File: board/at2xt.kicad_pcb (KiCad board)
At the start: 2 copper layers, 45.7 x 39.4 mm, 15 parts, among them J1 Conn_01x04, J2 XT, J3 AT, J4 PS/2, U1 MCP1700-3302E_TO92, U2 MSP430G2211IPW14

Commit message: Apply some suggestions from dragonmux's hoard.
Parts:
- moved C4 8.47 mm to (158.8, 64.8)
- moved C1 1.96 mm to (163.2, 62.2)
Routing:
- net +3.3V: track 73.4 -> 58.6 mm, vias 3 -> 2
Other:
- board text added: "TDIO VTGT TCK GND"
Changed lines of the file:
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@@
   )
   (footprint "Capacitor_SMD:C_0603_1608Metric" (layer "F.Cu")
-    (at 164.90942 58.955)
+    (at 158.75 64.77)
     (descr "Capacitor SMD 0603 (1608 Metric), square (rectangular) end terminal, IPC_7351 nominal, (Body size source: IPC-SM-782 page 76, https://www.pcb-3d.com/wordpress/wp-content/uploads/ipc-sm-782a_amendment_1_and_2.pdf), generated with kicad-footprint-generator")
     (tags "capacitor")
@@
   )
   (footprint "Capacitor_SMD:C_0603_1608Metric" (layer "F.Cu")
-    (at 165.1 61.955)
+    (at 163.16 62.23)
     (descr "Capacitor SMD 0603 (1608 Metric), square (rectangular) end terminal, IPC_7351 nominal, (Body size source: IPC-SM-782 page 76, https://www.pcb-3d.com/wordpress/wp-content/uploads/ipc-sm-782a_amendment_1_and_2.pdf), generated with kicad-footprint-generator")
     (tags "capacitor")
@@
   (gr_line (start 121.92 91.44) (end 167.64 91.44) (layer "Edge.Cuts") (width 0.1))
   (gr_line (start 167.64 91.44) (end 167.64 52.07) (layer "Edge.Cuts") (width 0.1))
-  (segment (start 164.465 64.135) (end 163.195 65.405) (width 0.25) (layer "F.Cu") (net 1))
-  (segment (start 163.195 65.405) (end 159.6525 65.405) (width 0.25) (layer "F.Cu") (net 1))
-  (segment (start 164.13442 58.955) (end 164.465 59.28558) (width 0.25) (layer "F.Cu") (net 1))
+  (gr_text "TDIO\nVTGT\nTCK\nGND" (at 129.54 64.135) (layer "B.SilkS")
+    (effects (font (size 1.5 1.5) (thickness 0.3)) (justify mirror))
+  )
+  (segment (start 159.245 63.5) (end 161.115 63.5) (width 0.25) (layer "F.Cu") (net 1))
+  (segment (start 157.975 66.1775) (end 158.4275 66.63) (width 0.25) (layer "F.Cu") (net 1))
+  (segment (start 160.335 60.6275) (end 160.335 61.91) (width 0.25) (layer "F.Cu") (net 1))
   (segment (start 130.62 64.2125) (end 130.62 67.31) (width 0.25) (layer "F.Cu") (net 1))
-  (segment (start 159.6525 65.405) (end 158.4275 66.63) (width 0.25) (layer "F.Cu") (net 1))
-  (segment (start 164.13442 56.18442) (end 164.13442 58.955) (width 0.25) (layer "F.Cu") (net 1))
   (segment (start 130.5 61.595) (end 130.5 64.0925) (width 0.25) (layer "F.Cu") (net 1))
-  (segment (start 160.335 61.91) (end 160.655 62.23) (width 0.25) (layer "F.Cu") (net 1))
-  (segment (start 164.465 59.28558) (end 164.465 64.135) (width 0.25) (layer "F.Cu") (net 1))
-  (segment (start 164.13442 56.18442) (end 163.83 55.88) (width 0.25) (layer "F.Cu") (net 1))
-  (segment (start 160.335 60.6275) (end 160.335 61.91) (width 0.25) (layer "F.Cu") (net 1))
+  (segment (start 157.975 64.77) (end 159.245 63.5) (width 0.25) (layer "F.Cu") (net 1))
   (segment (start 130.81 67.5) (end 130.62 67.31) (width 0.25) (layer "F.Cu") (net 1))
   (segment (start 132.08 59.055) (end 130.5 60.635) (width 0.25) (layer "F.Cu") (net 1))
   (segment (start 130.5 60.635) (end 130.5 61.595) (width 0.25) (layer "F.Cu") (net 1))
   (segment (start 128.0275 64.325) (end 126.555 64.325) (width 0.25) (layer "F.Cu") (net 1))
+  (segment (start 160.655 62.23) (end 162.385 62.23) (width 0.25) (layer "F.Cu") (net 1))
+  (segment (start 161.115 63.5) (end 162.385 62.23) (width 0.25) (layer "F.Cu") (net 1))
+  (segment (start 157.975 64.77) (end 157.975 66.1775) (width 0.25) (layer "F.Cu") (net 1))
   (segment (start 128.0275 64.325) (end 130.5075 64.325) (width 0.25) (layer "F.Cu") (net 1))
+  (segment (start 160.335 61.91) (end 160.655 62.23) (width 0.25) (layer "F.Cu") (net 1))
   (segment (start 130.5 64.0925) (end 130.62 64.2125) (width 0.25) (layer "F.Cu") (net 1))
   (segment (start 130.5075 64.325) (end 130.62 64.2125) (width 0.25) (layer "F.Cu") (net 1))
   (segment (start 130.81 69.85) (end 130.81 67.5) (width 0.25) (layer "F.Cu") (net 1))
   (segment (start 126.555 64.325) (end 125.095 62.865) (width 0.25) (layer "F.Cu") (net 1))
-  (via (at 163.83 55.88) (size 0.8) (drill 0.4) (layers "F.Cu" "B.Cu") (free) (net 1))
   (via (at 160.655 62.23) (size 0.8) (drill 0.4) (layers "F.Cu" "B.Cu") (free) (net 1))
   (via (at 132.08 59.055) (size 0.8) (drill 0.4) (layers "F.Cu" "B.Cu") (free) (net 1))
-  (segment (start 161.925 61.595) (end 161.925 57.15) (width 0.25) (layer "B.Cu") (net 1))
-  (segment (start 153.671396 60.96) (end 139.065 60.96) (width 0.25) (layer "B.Cu") (net 1))
+  (segment (start 139.065 60.96) (end 137.16 59.055) (width 0.25) (layer "B.Cu") (net 1))
   (segment (start 137.16 59.055) (end 132.08 59.055) (width 0.25) (layer "B.Cu") (net 1))
-  (segment (start 154.941396 62.23) (end 153.671396 60.96) (width 0.25) (layer "B.Cu") (net 1))
-  (segment (start 163.195 55.88) (end 163.83 55.88) (width 0.25) (layer "B.Cu") (net 1))
-  (segment (start 161.925 57.15) (end 163.195 55.88) (width 0.25) (layer "B.Cu") (net 1))
-  (segment (start 161.29 62.23) (end 161.925 61.595) (width 0.25) (layer "B.Cu") (net 1))
-  (segment (start 160.655 62.23) (end 161.29 62.23) (width 0.25) (layer "B.Cu") (net 1))
-  (segment (start 139.065 60.96) (end 137.16 59.055) (width 0.25) (layer "B.Cu") (net 1))
-  (segment (start 160.655 62.23) (end 154.941396 62.23) (width 0.25) (layer "B.Cu") (net 1))
+  (segment (start 154.94 60.96) (end 139.065 60.96) (width 0.25) (layer "B.Cu") (net 1))
+  (segment (start 160.655 62.23) (end 156.21 62.23) (width 0.25) (layer "B.Cu") (net 1))
+  (segment (start 156.21 62.23) (end 154.94 60.96) (width 0.25) (layer "B.Cu") (net 1))
   (segment (start 157.98558 58.00308) (end 158.75 58.7675) (width 0.25) (layer "F.Cu") (net 3))
   (segment (start 152.81 79.5) (end 150.2975 76.9875) (width 0.25) (layer "F.Cu") (net 3))

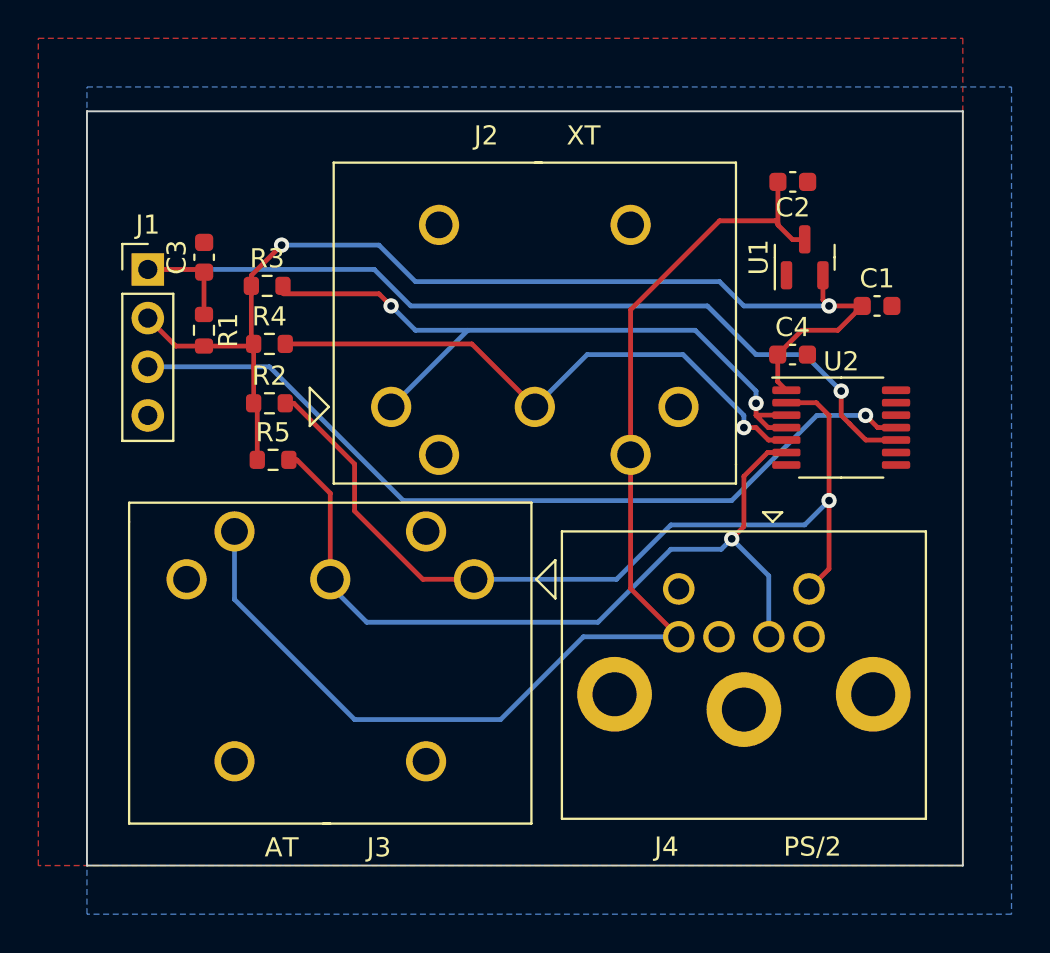
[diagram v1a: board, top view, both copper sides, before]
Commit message: Apply some more suggestions from dragonmux's hoard.
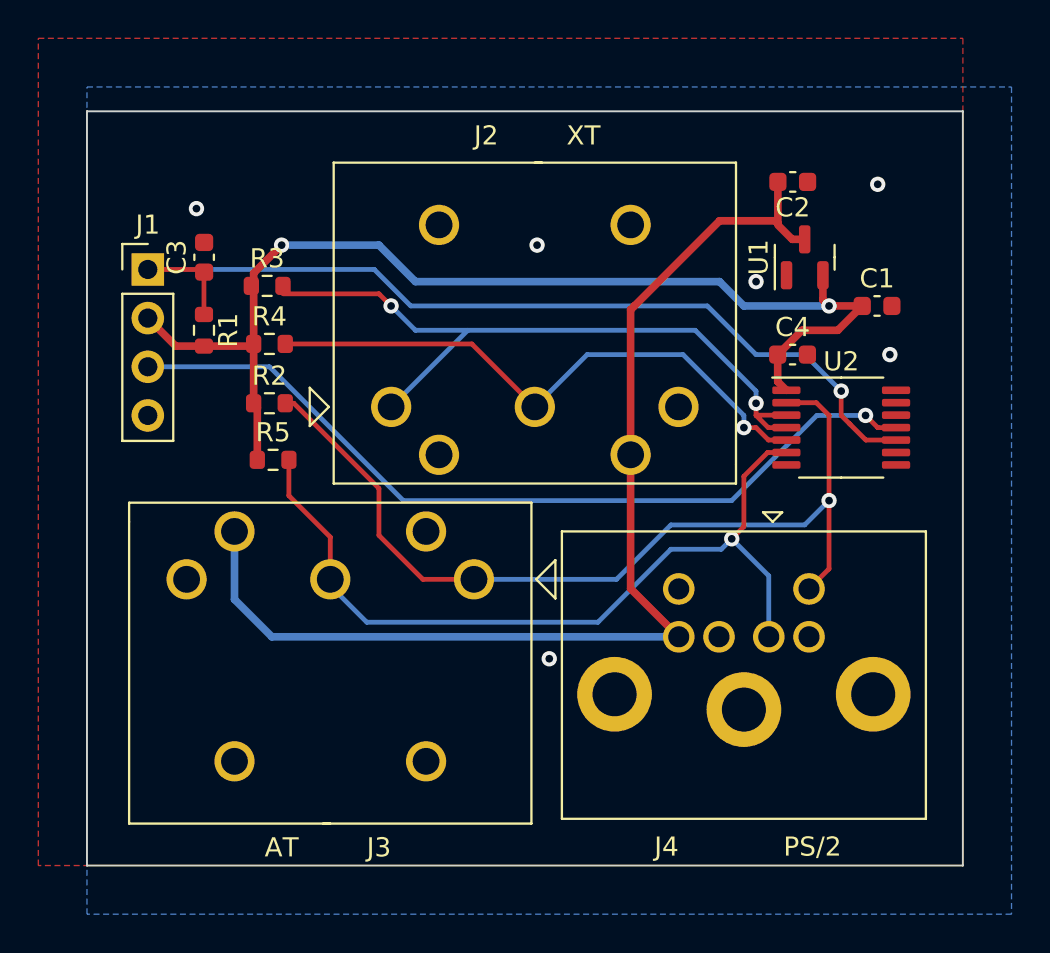
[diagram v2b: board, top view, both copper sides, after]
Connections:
- net /TCK renamed Net-(J1-Pad3)
- net /TDIO renamed Net-(C3-Pad1)
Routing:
- net +5V: track 62.9 -> 59.3 mm
- net +3.3V: track 58.6 -> 61.3 mm
- net GND: vias 0 -> 6

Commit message: Add .gitattributes for board folder, add name/version to silkscreen.
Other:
- board text added: "AT2XT v2.00 2023 WILLIAM D. JONES (CR1901)"
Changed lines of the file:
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@@
   (gr_line (start 121.92 91.44) (end 167.64 91.44) (layer "Edge.Cuts") (width 0.1))
   (gr_line (start 167.64 91.44) (end 167.64 52.07) (layer "Edge.Cuts") (width 0.1))
+  (gr_text "AT2XT v2.00 2023 WILLIAM D. JONES (CR1901)" (at 144.78 88.9) (layer "B.SilkS")
+    (effects (font (size 1 1) (thickness 0.25)) (justify mirror))
+  )
   (gr_text "TDIO\nVTGT\nTCK\nGND" (at 129.54 64.135) (layer "B.SilkS")
     (effects (font (size 1.5 1.5) (thickness 0.3)) (justify mirror))
